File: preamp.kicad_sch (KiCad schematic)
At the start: 16 parts, among them U3 THS4551

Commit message: Big commit for the day
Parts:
- renumbered C12 to 220p?, C13 to 220p?, C8 to C?, C7 to C?, C6 to C?, C9 to C?, CB5 to CB?, R13 to R?, R15 to R?, R17 to R?, R19 to R?, R14 to R?, R16 to R?, R18 to R?, R20 to R?, U3 to U?
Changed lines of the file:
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@@
   (symbol (lib_id "grootvoet:THS4551") (at 137.16 97.79 0) (unit 1)
     (in_bom yes) (on_board yes) (dnp no)
-    (property "Reference" "U3" (at 149.0218 108.9406 0)
+    (property "Reference" "U?" (at 149.0218 108.9406 0)
       (effects (font (size 1.27 1.27)))
     )
@@
   (symbol (lib_id "Device:C_Small") (at 163.83 97.79 0) (unit 1)
     (in_bom yes) (on_board yes) (dnp no)
-    (property "Reference" "CB5" (at 166.1668 96.6216 0)
+    (property "Reference" "CB?" (at 166.1668 96.6216 0)
       (effects (font (size 1.27 1.27)) (justify left))
     )
@@
   (symbol (lib_id "Device:R_Small") (at 99.06 80.01 270) (unit 1)
     (in_bom yes) (on_board yes) (dnp no)
-    (property "Reference" "R13" (at 99.06 75.0316 90)
+    (property "Reference" "R?" (at 99.06 75.0316 90)
       (effects (font (size 1.27 1.27)))
     )
@@
   (symbol (lib_id "Device:R_Small") (at 113.03 80.01 270) (unit 1)
     (in_bom yes) (on_board yes) (dnp no)
-    (property "Reference" "R15" (at 113.03 75.0316 90)
+    (property "Reference" "R?" (at 113.03 75.0316 90)
       (effects (font (size 1.27 1.27)))
     )
@@
   (symbol (lib_id "Device:R_Small") (at 149.86 69.85 270) (unit 1)
     (in_bom yes) (on_board yes) (dnp no)
-    (property "Reference" "R17" (at 149.86 64.8716 90)
+    (property "Reference" "R?" (at 149.86 64.8716 90)
       (effects (font (size 1.27 1.27)))
     )
@@
   (symbol (lib_id "Device:R_Small") (at 161.29 80.01 270) (unit 1)
     (in_bom yes) (on_board yes) (dnp no)
-    (property "Reference" "R19" (at 161.29 75.0316 90)
+    (property "Reference" "R?" (at 161.29 75.0316 90)
       (effects (font (size 1.27 1.27)))
     )
@@
   (symbol (lib_id "Device:C_Small") (at 143.51 80.01 270) (unit 1)
     (in_bom yes) (on_board yes) (dnp no)
-    (property "Reference" "C8" (at 143.51 74.1934 90)
+    (property "Reference" "C?" (at 143.51 74.1934 90)
       (effects (font (size 1.27 1.27)))
     )
@@
   (symbol (lib_id "Device:C_Small") (at 119.38 97.79 0) (unit 1)
     (in_bom yes) (on_board yes) (dnp no)
-    (property "Reference" "C7" (at 121.7168 96.6216 0)
+    (property "Reference" "C?" (at 121.7168 96.6216 0)
       (effects (font (size 1.27 1.27)) (justify left))
     )
@@
   (symbol (lib_id "Device:C_Small") (at 105.41 97.79 0) (unit 1)
     (in_bom yes) (on_board yes) (dnp no)
-    (property "Reference" "C6" (at 107.7468 96.6216 0)
+    (property "Reference" "C?" (at 107.7468 96.6216 0)
       (effects (font (size 1.27 1.27)) (justify left))
     )
@@
   (symbol (lib_id "Device:C_Small") (at 105.41 69.85 0) (unit 1)
     (in_bom yes) (on_board yes) (dnp no)
-    (property "Reference" "C12" (at 107.7468 68.6816 0)
+    (property "Reference" "220p?" (at 107.7468 68.6816 0)
       (effects (font (size 1.27 1.27)) (justify left))
     )
@@
   (symbol (lib_id "Device:R_Small") (at 99.06 115.57 270) (mirror x) (unit 1)
     (in_bom yes) (on_board yes) (dnp no)
-    (property "Reference" "R14" (at 99.06 120.5484 90)
+    (property "Reference" "R?" (at 99.06 120.5484 90)
       (effects (font (size 1.27 1.27)))
     )
@@
   (symbol (lib_id "Device:R_Small") (at 113.03 115.57 270) (mirror x) (unit 1)
     (in_bom yes) (on_board yes) (dnp no)
-    (property "Reference" "R16" (at 113.03 120.5484 90)
+    (property "Reference" "R?" (at 113.03 120.5484 90)
       (effects (font (size 1.27 1.27)))
     )
@@
   (symbol (lib_id "Device:R_Small") (at 149.86 125.73 270) (mirror x) (unit 1)
     (in_bom yes) (on_board yes) (dnp no)
-    (property "Reference" "R18" (at 149.86 130.7084 90)
+    (property "Reference" "R?" (at 149.86 130.7084 90)
       (effects (font (size 1.27 1.27)))
     )
@@
   (symbol (lib_id "Device:R_Small") (at 161.29 115.57 270) (mirror x) (unit 1)
     (in_bom yes) (on_board yes) (dnp no)
-    (property "Reference" "R20" (at 161.29 120.5484 90)
+    (property "Reference" "R?" (at 161.29 120.5484 90)
       (effects (font (size 1.27 1.27)))
     )
@@
   (symbol (lib_id "Device:C_Small") (at 143.51 115.57 270) (mirror x) (unit 1)
     (in_bom yes) (on_board yes) (dnp no)
-    (property "Reference" "C9" (at 143.51 121.3866 90)
+    (property "Reference" "C?" (at 143.51 121.3866 90)
       (effects (font (size 1.27 1.27)))
     )
@@
   (symbol (lib_id "Device:C_Small") (at 105.41 125.73 0) (mirror x) (unit 1)
     (in_bom yes) (on_board yes) (dnp no)
-    (property "Reference" "C13" (at 103.0732 124.5616 0)
+    (property "Reference" "220p?" (at 103.0732 124.5616 0)
       (effects (font (size 1.27 1.27)) (justify right))
     )

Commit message: (bc) large commit with spice experiments
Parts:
- gave numbers to parts that had none: 16

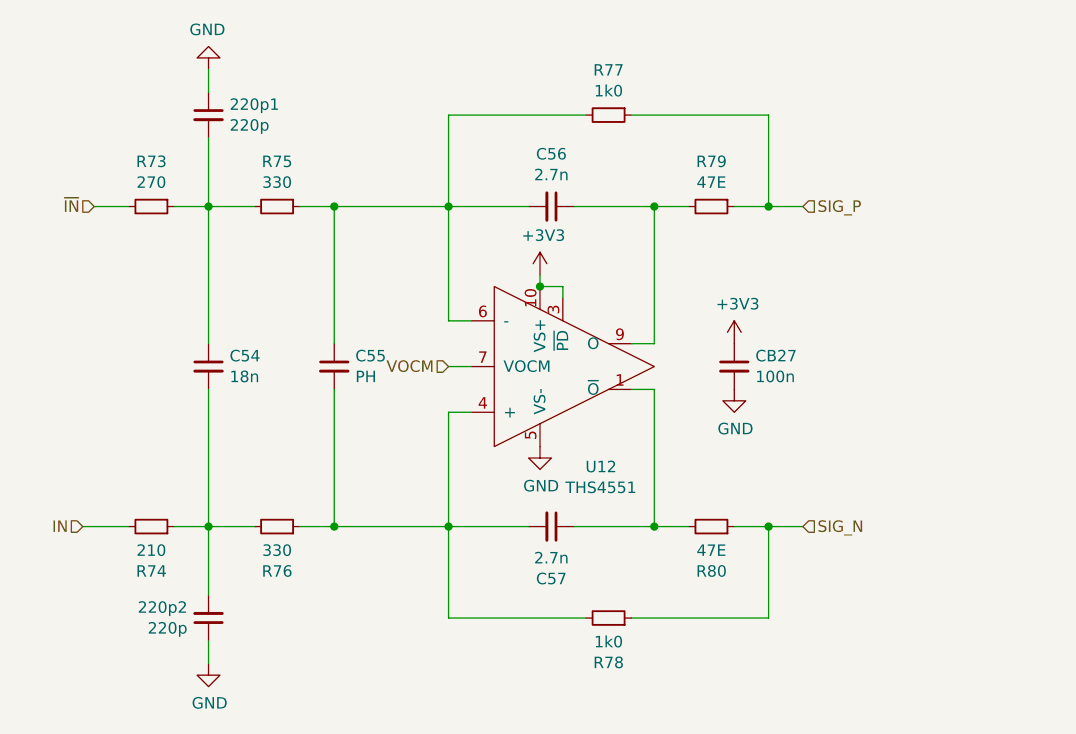
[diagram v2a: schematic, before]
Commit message: (bc) new summation preamp & seperate power net
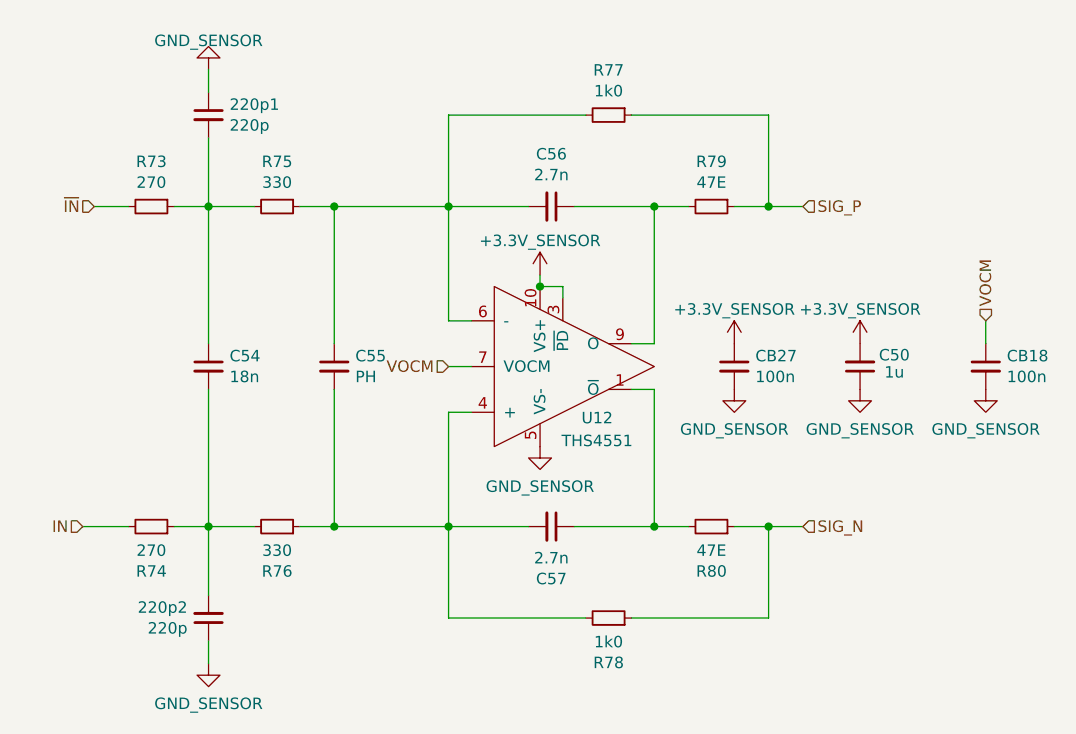
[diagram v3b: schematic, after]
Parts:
- added C50: 1u, Capacitor_SMD:C_0603_1608Metric_Pad1.08x0.95mm_HandSolder, symbol Device:C_Small
- added CB18: 100n, Capacitor_SMD:C_0603_1608Metric_Pad1.08x0.95mm_HandSolder, symbol Device:C_Small
- R74: value 210 -> 270; MPN ERJ-3EKF2100V -> (none)
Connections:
- net GND: now also C50.1, CB18.2
- net VOCM: now also CB18.1
- net +3V3 renamed +3.3V
- net +3.3V: now also C50.2

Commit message: (bc) changes for the day
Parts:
- removed R79, R80: 47E, Resistor_SMD:R_0603_1608Metric_Pad0.98x0.95mm_HandSolder, symbol Device:R_Small
- added R25 (x2): 15, Resistor_SMD:R_0603_1608Metric_Pad0.98x0.95mm_HandSolder, symbol Device:R_Small
- C55: now not fitted; now left out of the parts list
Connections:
- net SIG_N: now also R25.1
- net SIG_P: now also R25.1
- net at C57.1, U12.1 (~{O}): now also R25.2
- net at C56.1, U12.9 (O): now also R25.2
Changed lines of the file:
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@@
-    )
-  )
-  (symbol (lib_id "Device:R_Small") (at 161.29 80.01 270) (unit 1)
-    (in_bom yes) (on_board yes) (dnp no)
-    (property "Reference" "R79" (at 161.29 75.0316 90)
-      (effects (font (size 1.27 1.27)))
-    )
-    (property "Value" "47E" (at 161.29 77.343 90)
-      (effects (font (size 1.27 1.27)))
-    )
-    (property "Footprint" "Resistor_SMD:R_0603_1608Metric_Pad0.98x0.95mm_HandSolder" (at 161.29 80.01 0)
-      (effects (font (size 1.27 1.27)) hide)
-    )
-    (property "Datasheet" "~" (at 161.29 80.01 0)
-      (effects (font (size 1.27 1.27)) hide)
-    )
-    (property "Mfr." "Panasonic" (at 161.29 80.01 0)
-      (effects (font (size 1.27 1.27)) hide)
-    )
-    (property "MPN" "ERJ-3EKF47R0V" (at 161.29 80.01 0)
-      (effects (font (size 1.27 1.27)) hide)
-    )
-    (pin "1")
-    (pin "2")
-    (instances
-      (project "kleinvoet"
-        (path "/4185c36c-c66e-4dbd-be5d-841e551f4885/b53619ea-788f-4bc9-9946-594014d7d22c/00000000-0000-0000-0000-00005f9ed899"
-          (reference "R79") (unit 1)
-        )
-      )
-      (project "Sensor_Board"
-        (path "/7578b70c-b222-4cd3-b4ed-e0af47d4ab95"
-          (reference "R?") (unit 1)
-        )
-        (path "/7578b70c-b222-4cd3-b4ed-e0af47d4ab95/00000000-0000-0000-0000-00005f9ed899"
-          (reference "R19") (unit 1)
-        )
-      )
     )
   )
@@
   )
   (symbol (lib_id "Device:C_Small") (at 119.38 97.79 0) (unit 1)
-    (in_bom yes) (on_board yes) (dnp no)
+    (in_bom no) (on_board yes) (dnp yes)
     (property "Reference" "C55" (at 121.7168 96.6216 0)
       (effects (font (size 1.27 1.27)) (justify left))
@@
     )
   )
-  (symbol (lib_id "Device:R_Small") (at 161.29 115.57 270) (mirror x) (unit 1)
-    (in_bom yes) (on_board yes) (dnp no)
-    (property "Reference" "R80" (at 161.29 120.5484 90)
-      (effects (font (size 1.27 1.27)))
-    )
-    (property "Value" "47E" (at 161.29 118.237 90)
-      (effects (font (size 1.27 1.27)))
-    )
-    (property "Footprint" "Resistor_SMD:R_0603_1608Metric_Pad0.98x0.95mm_HandSolder" (at 161.29 115.57 0)
-      (effects (font (size 1.27 1.27)) hide)
-    )
-    (property "Datasheet" "~" (at 161.29 115.57 0)
-      (effects (font (size 1.27 1.27)) hide)
-    )
-    (property "Mfr." "Panasonic" (at 161.29 115.57 0)
-      (effects (font (size 1.27 1.27)) hide)
-    )
-    (property "MPN" "ERJ-3EKF47R0V" (at 161.29 115.57 0)
-      (effects (font (size 1.27 1.27)) hide)
-    )
-    (pin "1")
-    (pin "2")
-    (instances
-      (project "kleinvoet"
-        (path "/4185c36c-c66e-4dbd-be5d-841e551f4885/b53619ea-788f-4bc9-9946-594014d7d22c/00000000-0000-0000-0000-00005f9ed899"
-          (reference "R80") (unit 1)
-        )
-      )
-      (project "Sensor_Board"
-        (path "/7578b70c-b222-4cd3-b4ed-e0af47d4ab95"
-          (reference "R?") (unit 1)
-        )
-        (path "/7578b70c-b222-4cd3-b4ed-e0af47d4ab95/00000000-0000-0000-0000-00005f9ed899"
-          (reference "R20") (unit 1)
-        )
-      )
-    )
-  )
   (symbol (lib_id "Device:C_Small") (at 143.51 115.57 270) (mirror x) (unit 1)
     (in_bom yes) (on_board yes) (dnp no)
@@
     )
   )
+  (symbol (lib_id "Device:R_Small") (at 161.29 80.01 270) (mirror x) (unit 1)
+    (in_bom yes) (on_board yes) (dnp no)
+    (property "Reference" "R25" (at 161.29 75.0316 90)
+      (effects (font (size 1.27 1.27)))
+    )
+    (property "Value" "15" (at 161.29 77.343 90)
+      (effects (font (size 1.27 1.27)))
+    )
+    (property "Footprint" "Resistor_SMD:R_0603_1608Metric_Pad0.98x0.95mm_HandSolder" (at 161.29 80.01 0)
+      (effects (font (size 1.27 1.27)) hide)
+    )
+    (property "Datasheet" "~" (at 161.29 80.01 0)
+      (effects (font (size 1.27 1.27)) hide)
+    )
+    (property "MPN" "ERJ-3EKF15R0V" (at 161.29 80.01 0)
+      (effects (font (size 1.27 1.27)) hide)
+    )
+    (property "Mfr." "Panasonic" (at 161.29 80.01 0)
+      (effects (font (size 1.27 1.27)) hide)
+    )
+    (pin "1")
+    (pin "2")
+    (instances
+      (project "kleinvoet"
+        (path "/4185c36c-c66e-4dbd-be5d-841e551f4885/00000000-0000-0000-0000-00005ee5ecad/00000000-0000-0000-0000-00005ee62baf"
+          (reference "R25") (unit 1)
+        )
+        (path "/4185c36c-c66e-4dbd-be5d-841e551f4885/00000000-0000-0000-0000-00005ee5ecad/00000000-0000-0000-0000-00005ee91c90"
+          (reference "R49") (unit 1)
+        )
+        (path "/4185c36c-c66e-4dbd-be5d-841e551f4885/b53619ea-788f-4bc9-9946-594014d7d22c/00000000-0000-0000-0000-00005f9ed899"
+          (reference "R108") (unit 1)
+        )
+      )
+    )
+  )
   (symbol (lib_id "grootvoet:+3.3V_SENSOR") (at 142.24 87.63 0) (unit 1)
     (in_bom yes) (on_board yes) (dnp no) (fields_autoplaced)
@@
         )
       )
+    )
+  )
+  (symbol (lib_id "Device:R_Small") (at 161.29 115.57 270) (mirror x) (unit 1)
+    (in_bom yes) (on_board yes) (dnp no)
+    (property "Reference" "R25" (at 161.29 110.5916 90)
+      (effects (font (size 1.27 1.27)))
+    )
+    (property "Value" "15" (at 161.29 112.903 90)
+      (effects (font (size 1.27 1.27)))
+    )
+    (property "Footprint" "Resistor_SMD:R_0603_1608Metric_Pad0.98x0.95mm_HandSolder" (at 161.29 115.57 0)
+      (effects (font (size 1.27 1.27)) hide)
+    )
+    (property "Datasheet" "~" (at 161.29 115.57 0)
+      (effects (font (size 1.27 1.27)) hide)
+    )
+    (property "MPN" "ERJ-3EKF15R0V" (at 161.29 115.57 0)
+      (effects (font (size 1.27 1.27)) hide)
+    )
+    (property "Mfr." "Panasonic" (at 161.29 115.57 0)
+      (effects (font (size 1.27 1.27)) hide)
+    )
+    (pin "1")
+    (pin "2")
+    (instances
+      (project "kleinvoet"
+        (path "/4185c36c-c66e-4dbd-be5d-841e551f4885/00000000-0000-0000-0000-00005ee5ecad/00000000-0000-0000-0000-00005ee62baf"
+          (reference "R25") (unit 1)
+        )
+        (path "/4185c36c-c66e-4dbd-be5d-841e551f4885/00000000-0000-0000-0000-00005ee5ecad/00000000-0000-0000-0000-00005ee91c90"
+          (reference "R49") (unit 1)
+        )
+        (path "/4185c36c-c66e-4dbd-be5d-841e551f4885/b53619ea-788f-4bc9-9946-594014d7d22c/00000000-0000-0000-0000-00005f9ed899"
+          (reference "R109") (unit 1)
+        )
+      )

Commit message: (sch) relabel
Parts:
- renumbered 220p1 to 220p1501, 220p2 to 220p1502, C54 to C1501, C55 to C1502, C56 to C1503, C57 to C1504, C50 to C1505, CB27 to CB1501, R73 to R1501, R74 to R1502, R75 to R1503, R76 to R1504, R77 to R1505, R78 to R1506, U12 to U1501

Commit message: (hk) asign footprints
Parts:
- renumbered 220p1501 to 220p1601, 220p1502 to 220p1602, C1501 to C1601, C1502 to C1602, C1503 to C1603, C1504 to C1604, C1505 to C1605, CB1501 to CB1601, R1501 to R1601, R1502 to R1602, R1503 to R1603, R1504 to R1604, R1505 to R1605, R1506 to R1606, U1501 to U1601

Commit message: (sch) change passives to 0402
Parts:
- C1601: footprint Capacitor_SMD:C_0603_1608Metric_Pad1.08x0.95mm_HandSolder -> Capacitor_SMD:C_0603_1608Metric; MPN CC0603JRX7R8BB183 -> C1608C0G1V183J080AC; Mfr. Yageo -> TDK
- C1603, C1604: footprint Capacitor_SMD:C_0603_1608Metric_Pad1.08x0.95mm_HandSolder -> Capacitor_SMD:C_0402_1005Metric; MPN CC0603JRX7R9BB272 -> GRM1555C1H272GE01D; Mfr. Yageo -> Murata
- C1605: MPN (none) -> C0603C105K8RACTU; Mfr. (none) -> KEMET
- C?: renamed from 220p1601; footprint Capacitor_SMD:C_0603_1608Metric_Pad1.08x0.95mm_HandSolder -> Capacitor_SMD:C_0402_1005Metric; MPN C0603C221J5GACTU -> GRT1555C1H221FA02D; Mfr. KEMET -> Murata
- C?: renamed from 220p1602; footprint Capacitor_SMD:C_0603_1608Metric_Pad1.08x0.95mm_HandSolder -> Capacitor_SMD:C_0402_1005Metric; MPN C0603C221J5GACTU -> GRT1555C1H221FA02D; Mfr. KEMET -> Murata
- R1601: footprint Resistor_SMD:R_0603_1608Metric_Pad0.98x0.95mm_HandSolder -> Resistor_SMD:R_0402_1005Metric; MPN ERJ-3EKF2700V -> RT0402FRE07270RL; Mfr. Panasonic -> Yageo
- R1602: footprint Resistor_SMD:R_0603_1608Metric_Pad0.98x0.95mm_HandSolder -> Resistor_SMD:R_0402_1005Metric; MPN (none) -> RT0402FRE07270RL; Mfr. Panasonic -> Yageo
- R1603, R1604: value 330 -> 330E; footprint Resistor_SMD:R_0603_1608Metric_Pad0.98x0.95mm_HandSolder -> Resistor_SMD:R_0402_1005Metric; MPN ERJ-3EKF3300V -> RT0402FRE07330RL; Mfr. Panasonic -> Yageo
- R1605, R1606: value 1k0 -> 1k; footprint Resistor_SMD:R_0603_1608Metric_Pad0.98x0.95mm_HandSolder -> Resistor_SMD:R_0402_1005Metric; MPN ERJ-3EKF1001V -> RT0402FRE071KL; Mfr. Panasonic -> Yageo
- R25: value 15 -> 14.7E; footprint Resistor_SMD:R_0603_1608Metric_Pad0.98x0.95mm_HandSolder -> Resistor_SMD:R_0402_1005Metric; MPN ERJ-3EKF15R0V -> RT0603FRE0714R7L; Mfr. Panasonic -> Yageo

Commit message: (pcb) initial layout
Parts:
- CB1601, CB18: footprint Capacitor_SMD:C_0603_1608Metric_Pad1.08x0.95mm_HandSolder -> Capacitor_SMD:C_0402_1005Metric; MPN C0603C104M5RACTU -> C0402C104K8PACTU
- gave numbers to parts that had none: 2
